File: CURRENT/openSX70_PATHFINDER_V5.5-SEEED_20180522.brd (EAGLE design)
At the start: 95.9 x 27.9 mm, 41 parts, among them J1 687106183722, Q1 5.8A/30V/35mΩ, Q2 5.8A/30V/35mΩ, U1 ATMEGA328P_TQFP, U3 BH1750FVI-TR, Y1 CSTCE8M00G52Z-R0

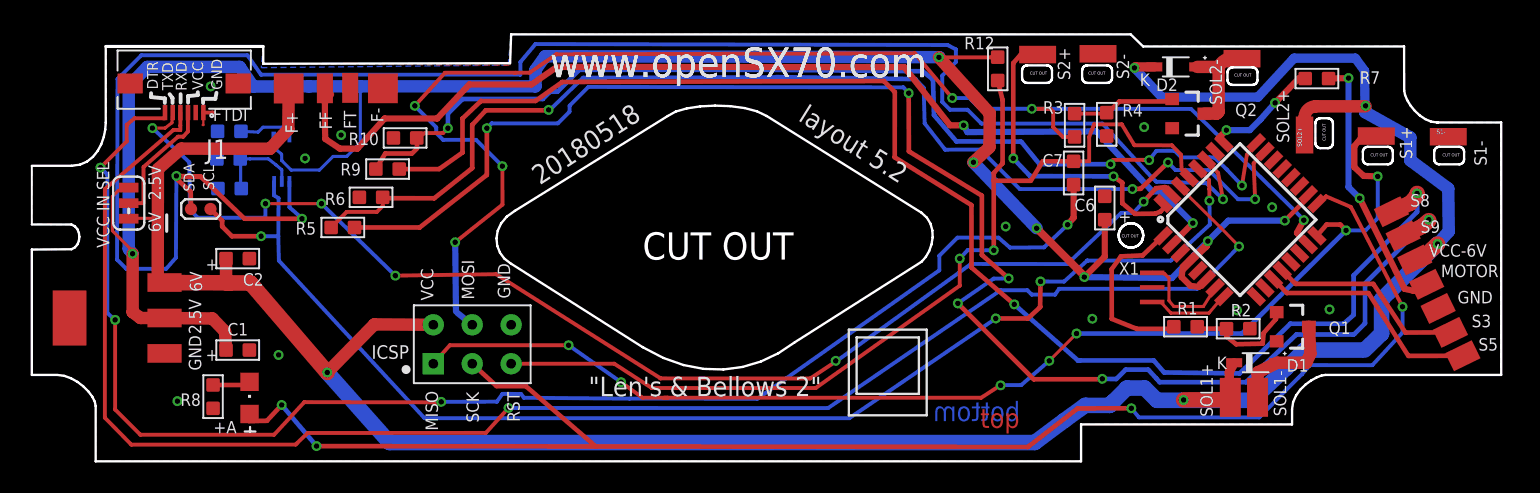
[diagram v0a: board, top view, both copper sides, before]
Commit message: New 5,5 "Pathfinder" with relocated BH1750 and removed buzzer.
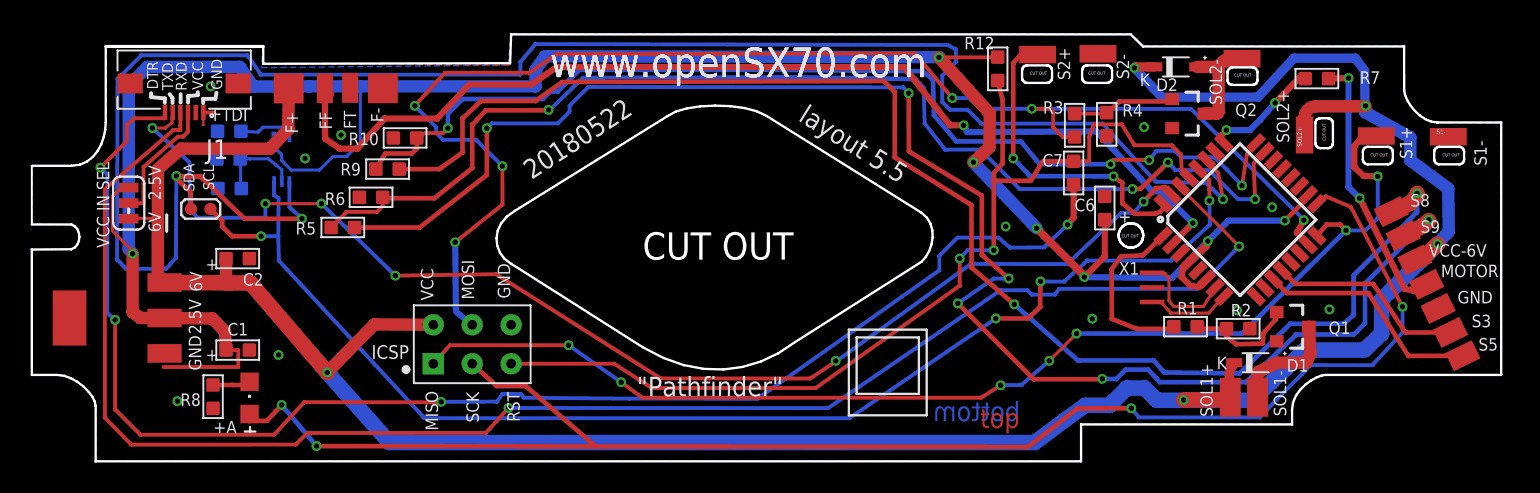
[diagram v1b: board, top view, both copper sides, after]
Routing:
- net 3.3V: track 149.0 -> 155.8 mm
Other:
- board text added: ""Pathfinder""
- board text added: "20180522"
- board text added: "openSX70 project visit www.openSX70.com version 5.5 "Pathfinder" 20170522 by Joaquín de Prada"
- board text removed: ""Len's & Bellows 2""
- board text removed: "20180518"
- board text removed: "layout 5.2"
- board text removed: "openSX70 project visit www.openSX70.com version 5.5 "Len's & Bellows 2" 20170518 by Joaquín de Prada"
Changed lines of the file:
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@@
 https://creativecommons.org/licenses/by-nc/4.0/</text>
 <text x="35.8775" y="25.87625" size="1.9304" layer="21" font="vector" ratio="15">www.openSX70.com</text>
-<text x="41.2115" y="24.22525" size="1.27" layer="21" font="vector" ratio="15" rot="R213">20180518</text>
-<text x="52.0065" y="23.08225" size="1.27" layer="21" font="vector" ratio="15" rot="R328">layout 5.2</text>
+<text x="40.6615" y="24.57525" size="1.27" layer="21" font="vector" ratio="15" rot="R213">20180522</text>
+<text x="52.0065" y="23.08225" size="1.27" layer="21" font="vector" ratio="15" rot="R328">layout 5.5</text>
 <text x="96.4565" y="8.03275" size="0.8128" layer="21" font="vector" ratio="20">S5</text>
 <text x="95.09125" y="11.1125" size="0.8128" layer="21" font="vector" ratio="20">GND</text>
@@
 <text x="15.42975" y="2.62575" size="0.8128" layer="25" font="vector" ratio="20" rot="MR0">A+</text>
 <text x="79.72425" y="24.0665" size="0.8128" layer="21" font="vector" ratio="20" rot="R90">SOL2-</text>
-<text x="53.6575" y="5.17525" size="1.27" layer="22" font="vector" ratio="15" rot="MR0">"Len's &amp; Bellows 2"</text>
+<text x="51.7075" y="5.02525" size="1.27" layer="22" font="vector" ratio="15" rot="MR0">"Pathfinder"</text>
 <text x="35.8775" y="25.87625" size="1.9304" layer="21" font="vector" ratio="15">www.openSX70.com</text>
 <text x="59.6265" y="25.74925" size="1.9304" layer="22" font="vector" ratio="15" rot="MR0">www.openSX70.com</text>
@@
 <text x="66.548" y="3.429" size="1.27" layer="16" font="vector" ratio="15" rot="MR0">bottom</text>
 <text x="48.9585" y="-4.66725" size="1.778" layer="51" align="center">openSX70 project visit www.openSX70.com
-version 5.5 "Len's &amp; Bellows 2" 20170518
+version 5.5 "Pathfinder" 20170522
 by Joaquín de Prada</text>
 <text x="36.957" y="16.383" size="1.778" layer="51" font="vector">ALL VIAS TENTED</text>
@@
 <wire x1="59.944" y1="5.207" x2="55.88" y2="5.207" width="0.1524" layer="21"/>
 <wire x1="55.88" y1="5.207" x2="55.88" y2="8.89" width="0.1524" layer="21"/>
-<text x="38.3835" y="5.05275" size="1.27" layer="21" font="vector" ratio="15">"Len's &amp; Bellows 2"</text>
+<text x="41.5335" y="5.05275" size="1.27" layer="21" font="vector" ratio="15">"Pathfinder"</text>
 <wire x1="12.065" y1="17.907" x2="14.097" y2="17.907" width="0.1524" layer="21"/>
 <wire x1="14.097" y1="17.907" x2="14.351" y2="17.653" width="0.1524" layer="21"/>
@@
 <wire x1="78.8035" y1="15.1765" x2="80.137" y2="16.51" width="0.4064" layer="16"/>
 <wire x1="80.137" y1="16.51" x2="83.82" y2="16.51" width="0.4064" layer="16"/>
+<wire x1="14.732" y1="8.0645" x2="15.5321" y2="8.0645" width="0.254" layer="1"/>
+<wire x1="15.5321" y1="8.0645" x2="15.5321" y2="6.9596" width="0.254" layer="1"/>
+<wire x1="15.5321" y1="6.9596" x2="10.65" y2="6.9596" width="0.254" layer="1"/>
 </signal>
 <signal name="GND">
@@
 <contactref element="R8" pad="2"/>
 <contactref element="LED1" pad="C"/>
-<wire x1="13.885" y1="5.788" x2="16.058" y2="5.788" width="0.3048" layer="1"/>
+<wire x1="13.885" y1="5.788" x2="15.15" y2="5.788" width="0.3048" layer="1"/>
+<wire x1="15.15" y1="5.788" x2="16.058" y2="5.788" width="0.3048" layer="1"/>
 <wire x1="16.058" y1="5.788" x2="16.265" y2="5.995" width="0.3048" layer="1"/>
 </signal>

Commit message: Pathfinder
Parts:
- moved R13 0.20 mm to (15.1, 20.5)
- moved C5 0.18 mm to (15.1, 18.7)
- moved R14 0.15 mm to (15.1, 22.3)
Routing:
- net 3.3V: track 155.8 -> 148.7 mm
- net 6V: track 189.9 -> 191.3 mm
